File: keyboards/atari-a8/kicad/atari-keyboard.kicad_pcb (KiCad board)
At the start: 2 copper layers, 357.2 x 140.5 mm, 162 parts, among them J101 PLAYER 1, J103 I2C DISPLAY, SW200 ESC, SW201 1, SW202 2, SW203 3, SW204 4, SW205 5, SW206 6, SW207 7, SW208 8, SW209 9, SW210 0, SW211 LT, SW212 GT, SW213 BS, SW214 C_UP, SW215 C_LEFT, SW216 C_DOWN, SW217 C_RIGHT, SW218 TAB, SW219 Q, SW220 W, SW221 E, SW222 R, SW223 T, SW224 Y, SW225 U, SW226 I, SW227 O, SW228 P, SW229 DASH, SW230 EQUAL, SW231 RETURN, SW232 HELP, SW233 RESET, SW234 OPTION, SW235 SELECT, SW236 CONTROL, SW237 A, SW238 S, SW239 D, SW240 F, SW241 G, SW242 H, SW243 J, SW244 K, SW245 L, SW246 SEMI, SW247 PLUS, SW248 ASTRIX, SW249 CAPS, SW250 START, SW251 POWER, SW252 MENU, SW253 TURBO, SW254 FN, SW255 LSHIFT, SW256 Z, SW257 X, SW258 C, SW259 V, SW260 B, SW261 N, SW262 M, SW268 COMMA, SW269 PERIOD, SW270 SLASH, SW271 RSHIFT, SW277 INV, SW278 BREAK, SW279 SPACE, U101 Elite-C, U102 MAX7219, U103 MAX7219

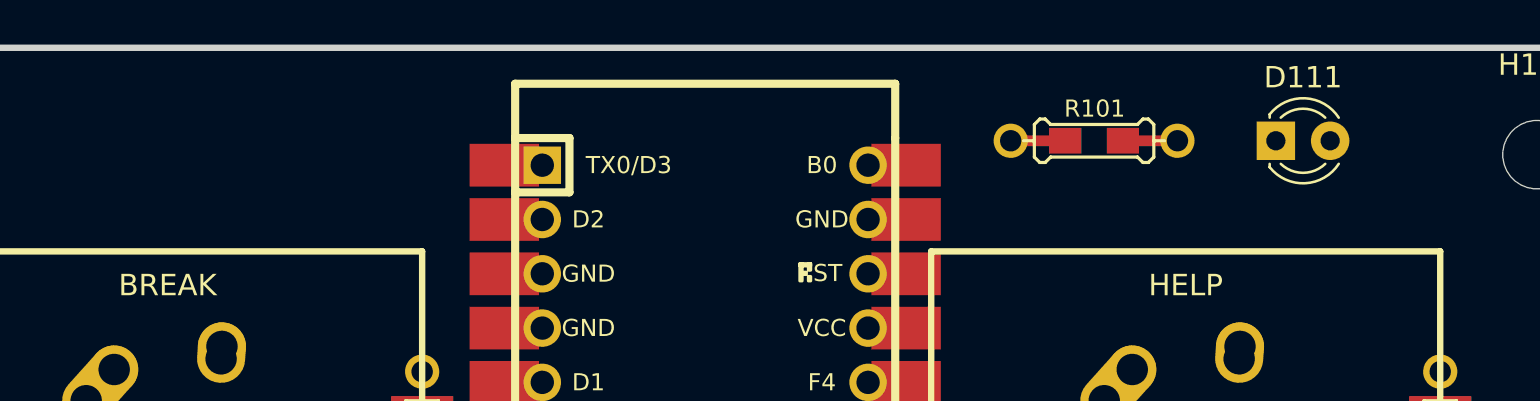
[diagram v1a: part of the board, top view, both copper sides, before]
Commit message: Added some tweaks learned working on keyboard prototype
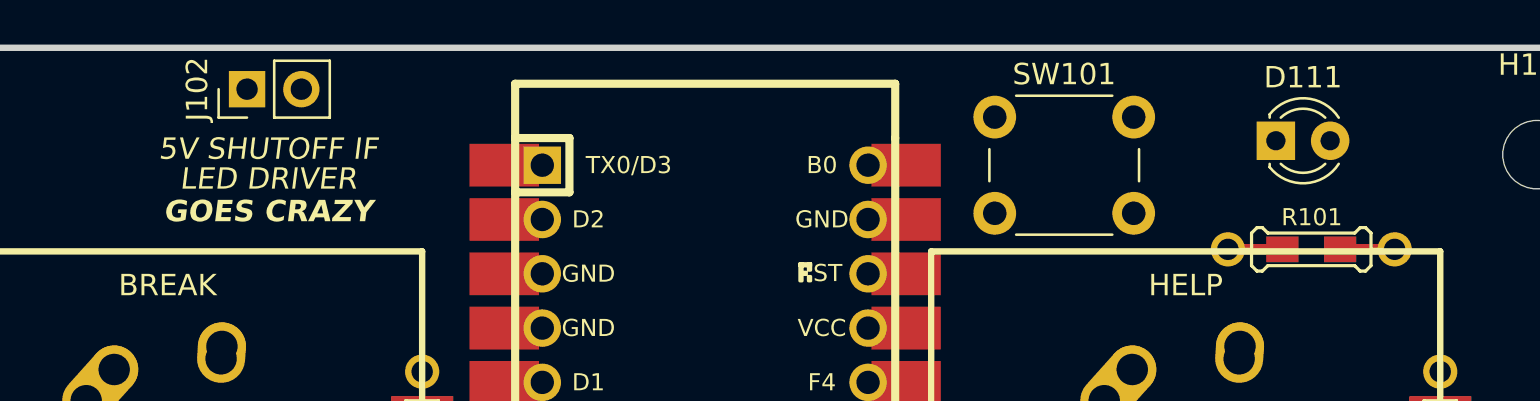
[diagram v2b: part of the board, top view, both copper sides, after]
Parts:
- added J102: 5V, Connector_PinHeader_2.54mm:PinHeader_1x02_P2.54mm_Vertical, F.Cu at (310.9, 156.7)
- added SW101: RESET, Button_Switch_THT:SW_PUSH_6mm, F.Cu at (345.9, 158.0)
- moved R101 11.4 mm to (360.7, 164.2)
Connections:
- D105 pad 2: unconnected-(D105-A-Pad2) -> SW_COL5
- J101 pad 7: /JS1_+5 -> VCC
- U101 pad 21: VCC -> Net-(J102-Pin_2)
- U101 pad 22: unconnected-(U101-RST-Pad22) -> RST
- U102 pad 13: SW_COL5 -> SW_COL1
- U103 pad 1: SW_COL6 -> SW_COL3
- U103 pad 13: SW_COL5 -> SW_COL1
